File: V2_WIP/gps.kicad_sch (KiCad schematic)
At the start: 33 parts, among them U10 24C32, U101 DFR0654, U102 W25Q128JFV, U2 TPS613222ADBVR

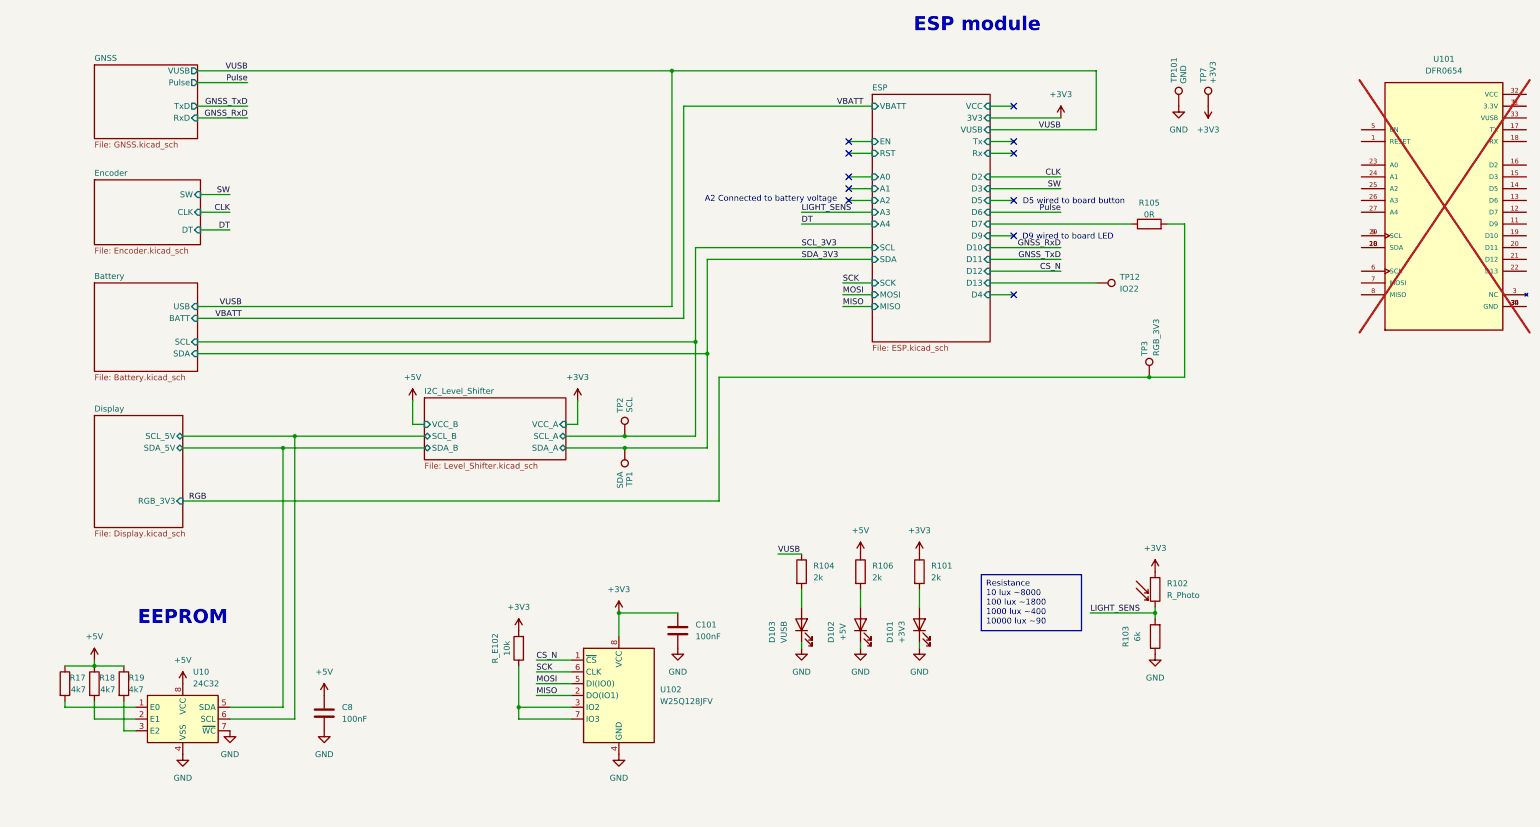
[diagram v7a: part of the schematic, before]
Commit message: fixed errors in schematic
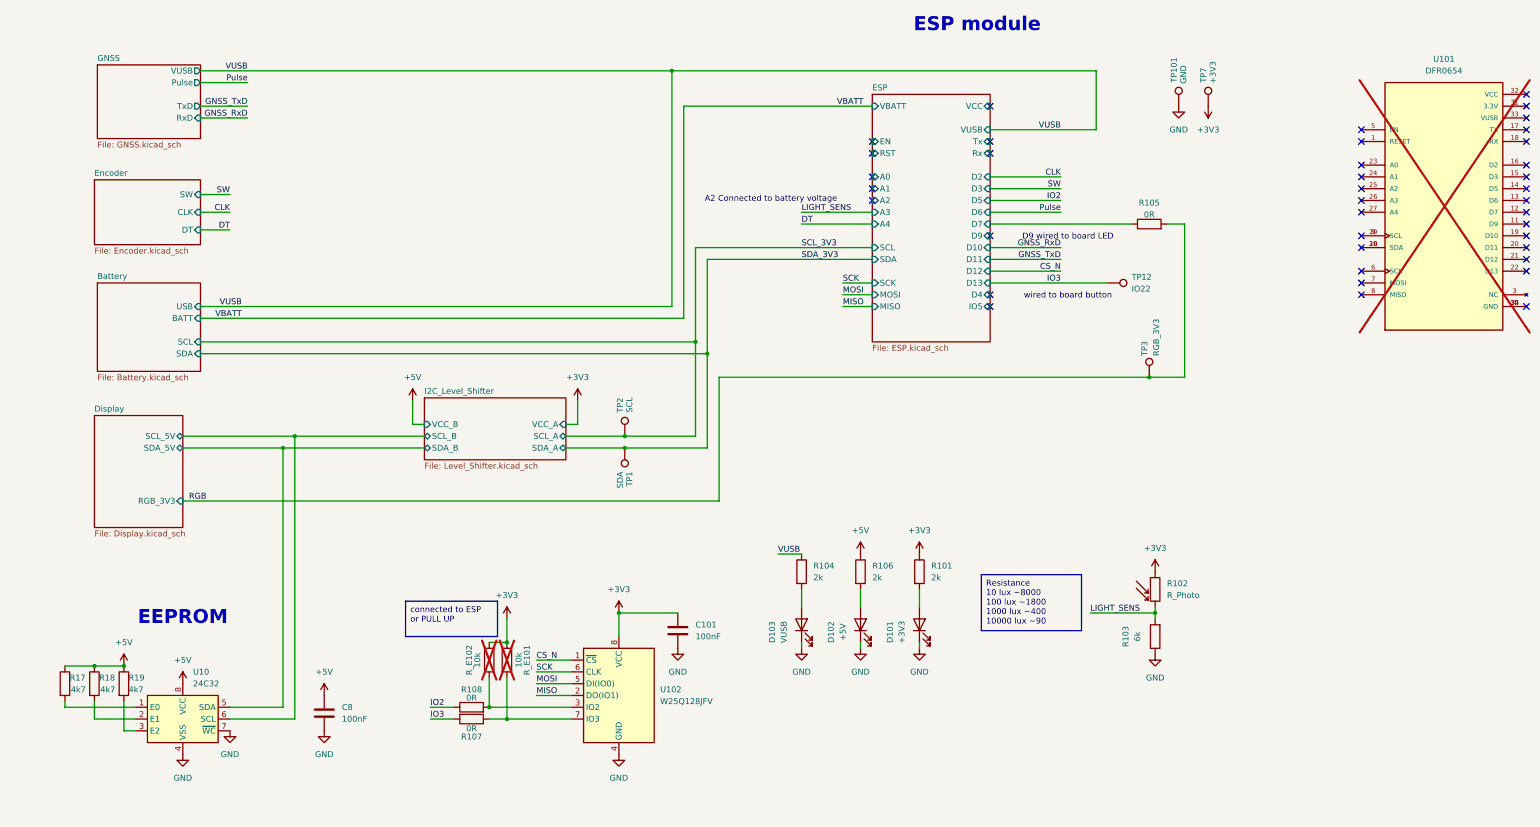
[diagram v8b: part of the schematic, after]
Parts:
- added R107, R108: 0R, Resistor_SMD:R_0603_1608Metric_Pad0.98x0.95mm_HandSolder, symbol Device:R
- added R_E101: 10k, Resistor_SMD:R_0603_1608Metric_Pad0.98x0.95mm_HandSolder, symbol Device:R
- R17, R18, R19: footprint Resistor_SMD:R_0805_2012Metric_Pad1.20x1.40mm_HandSolder -> Resistor_SMD:R_0603_1608Metric_Pad0.98x0.95mm_HandSolder
- R_E102: footprint Resistor_SMD:R_0805_2012Metric_Pad1.20x1.40mm_HandSolder -> Resistor_SMD:R_0603_1608Metric_Pad0.98x0.95mm_HandSolder; now not fitted
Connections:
- net +3V3: now also R_E101.1
- net at R_E102.1, U102.3 (IO2): now also R108.2; no longer U102.7 (IO3)
- net ESP/D13 renamed IO3
- net IO3: now also R107.2
- new net: R107.1, R_E101.2, U102.7 (IO3)
- new net IO2: R108.1
- no-connect marks 11 -> 39
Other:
- sheet ESP ports: added IO5; removed 3V3
- note added: "wired to board button"
- note removed: "D5 wired to board button"
- moved on the sheet: TP12
